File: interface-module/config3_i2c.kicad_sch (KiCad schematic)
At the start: 9 parts, among them U301 TCA9548

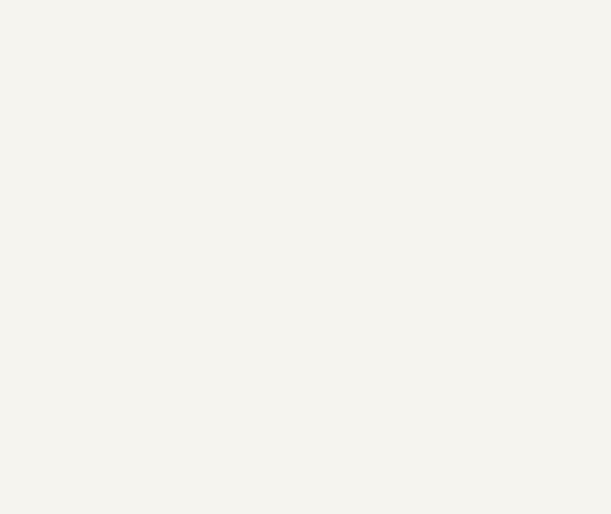
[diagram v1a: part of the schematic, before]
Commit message: Added LEDs for outputs and improved silkscreen
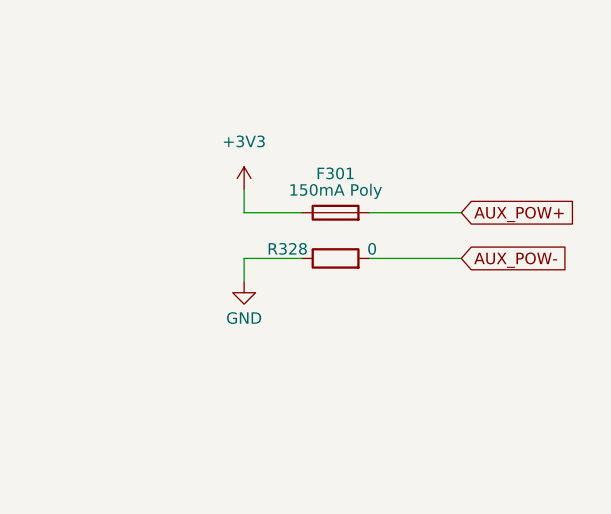
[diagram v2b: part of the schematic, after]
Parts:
- added F301: 150mA Poly, Fuse:Fuse_1206_3216Metric, symbol Device:Fuse
- added R328: 0, Resistor_SMD:R_0603_1608Metric, symbol Device:R
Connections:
- net +3V3: now also F301.1
- net GND: now also R328.1
- new net AUX_POW+: F301.2
- new net AUX_POW-: R328.2

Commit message: Fixed BOM issues
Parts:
- C301: MPN CL10A105KL8NNNC -> CL10A105KL8NNNC
- R304, R305: MPN RMCF0603FT4k70 -> RMCF0603FT4K70
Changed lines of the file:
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@@
 			)
 		)
-		(property "MPN" "RMCF0603FT4k70"
+		(property "MPN" "RMCF0603FT4K70"
 			(at 176.53 105.41 0)
 			(effects
@@
 			)
 		)
-		(property "MPN" "CL10A105KL8NNNC "
+		(property "MPN" "CL10A105KL8NNNC"
 			(at 233.68 152.4 0)
 			(effects
@@
 			)
 		)
-		(property "MPN" "RMCF0603FT4k70"
+		(property "MPN" "RMCF0603FT4K70"
 			(at 171.45 105.41 0)
 			(effects

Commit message: Upgraded to v1.1.
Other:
- company: (none) -> Portland State Aerosapce Society
- title: (none) -> MinTS Interface Module
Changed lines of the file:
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@@
 	(generator_version "9.0")
 	(paper "USLedger")
+	(title_block
+		(title "MinTS Interface Module")
+		(date "2025-12-23")
+		(rev "1.1")
+		(company "Portland State Aerosapce Society")
+	)
 	(junction
 		(at 204.47 114.3)

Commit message: Final polish before manufacturing (v1.1)
Upped version to 1.1. Cleared ERC errors, one interesting one left that won't stop manufacturing. Cleared all DRC warnings and
errors. Formatted BOM. Fixed BOM for important parts. Added fuse parts for reference. Cleaned up silkscreen.
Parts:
- C301, R301, R302, R303, R304, R305, R328, U301: DIS (none) -> DigiKey
- F301: DIS (none) -> DigiKey; MFR (none) -> Littelfuse
- RN301, RN302: DIS (none) -> DigiKey; MFR (none) -> Bourns
